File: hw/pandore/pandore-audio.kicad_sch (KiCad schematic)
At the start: 1 part, among them U9 Teensy 4.1

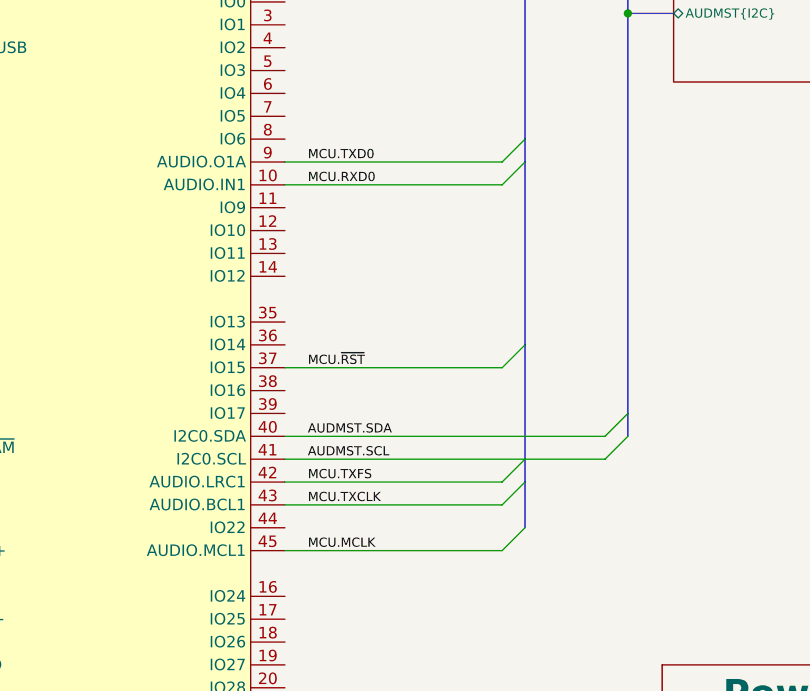
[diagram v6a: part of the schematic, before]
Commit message: lots of routing (diff, buses, power) done optimised buffer out
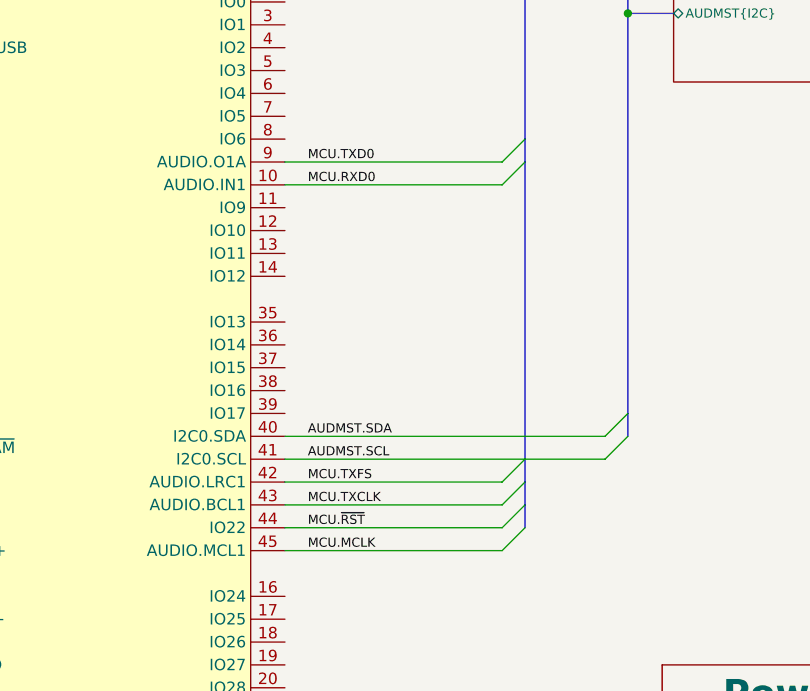
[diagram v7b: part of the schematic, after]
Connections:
- net MCU.~{RST}: now also U9.44 (IO22); no longer U9.37 (IO15)
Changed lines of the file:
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@@
 	)
 	(bus_entry
-		(at 107.95 110.49)
+		(at 107.95 128.27)
 		(size 2.54 -2.54)
 		(stroke
@@
 	(bus
 		(pts
-			(xy 110.49 107.95) (xy 110.49 120.65)
-		)
-		(stroke
-			(width 0)
-			(type default)
-		)
-	)
-	(bus
-		(pts
 			(xy 31.75 60.96) (xy 127 60.96)
 		)
@@
 	(wire
 		(pts
-			(xy 83.82 110.49) (xy 107.95 110.49)
+			(xy 83.82 128.27) (xy 107.95 128.27)
 		)
 		(stroke
@@
 	(bus
 		(pts
+			(xy 110.49 125.73) (xy 110.49 128.27)
+		)
+		(stroke
+			(width 0)
+			(type default)
+		)
+	)
+	(bus
+		(pts
 			(xy 220.98 59.69) (xy 238.76 59.69)
 		)
@@
 	(bus
 		(pts
-			(xy 110.49 87.63) (xy 110.49 107.95)
+			(xy 110.49 87.63) (xy 110.49 120.65)
 		)
 		(stroke
@@
 	(bus
 		(pts
-			(xy 110.49 123.19) (xy 110.49 128.27)
+			(xy 110.49 123.19) (xy 110.49 125.73)
 		)
 		(stroke
@@
 	)
 	(label "MCU.~{RST}"
-		(at 86.36 110.49 0)
-		(effects
-			(font
+		(at 86.36 128.27 0)
+		(effects
+			(font

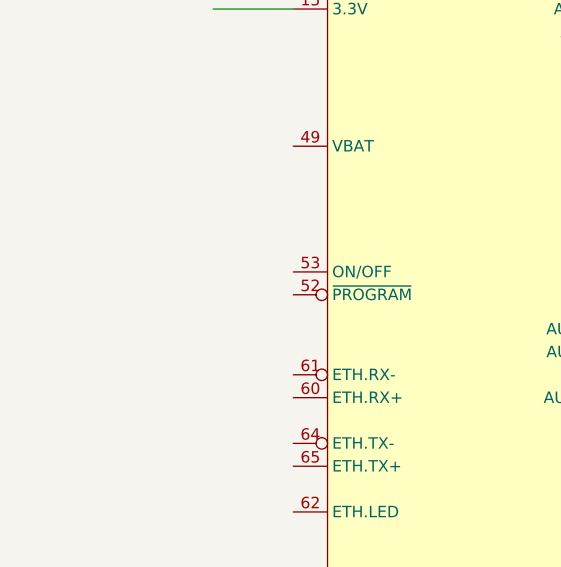
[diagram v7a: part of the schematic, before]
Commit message: lcd control circuit added fan interface added rgba output pinout for management mcu accessories done
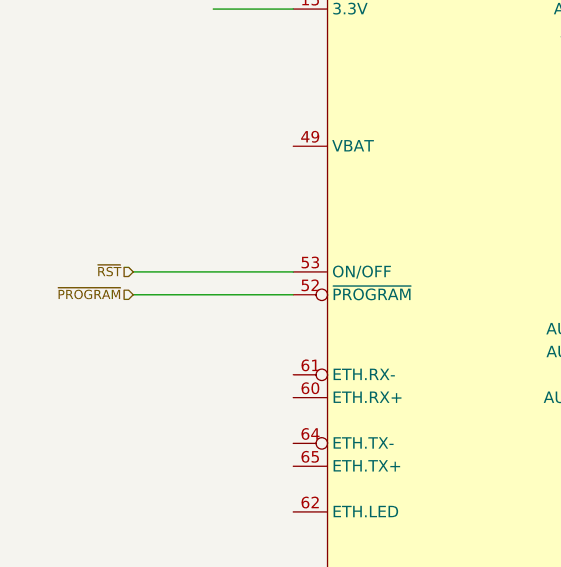
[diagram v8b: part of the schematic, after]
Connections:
- net ~{PROGRAM}: now reaches U9.52 (~{PROGRAM})
- net ~{RST}: now reaches U9.53 (ON/OFF)
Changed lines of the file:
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@@
+	(wire
+		(pts
+			(xy 22.86 119.38) (xy 40.64 119.38)
+		)
+		(stroke
+			(width 0)
+			(type default)
+		)
+	)
 	(wire
 		(pts
@@
 		(pts
 			(xy 121.92 115.57) (xy 121.92 118.11)
+		)
+		(stroke
+			(width 0)
+			(type default)
+		)
+	)
+	(wire
+		(pts
+			(xy 22.86 116.84) (xy 40.64 116.84)
 		)
 		(stroke
@@
 		(effects
 			(font
+				(size 1.016 1.016)
+			)
+			(justify right)
+		)
+	)
+	(hierarchical_label "~{RST}"
+		(shape input)
+		(at 22.86 116.84 180)
+		(effects
+			(font
+				(size 1.016 1.016)
+			)
+			(justify right)
+		)
+	)
+	(hierarchical_label "~{PROGRAM}"
+		(shape input)
+		(at 22.86 119.38 180)
+		(effects
+			(font
